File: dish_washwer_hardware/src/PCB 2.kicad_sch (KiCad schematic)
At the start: 25 parts, among them J18 Conn_02x07_Odd_Even, J19 SCREEN CONNECTOR, J20 Conn_01x10_Male, U12 TXS0108EPW, U13 EAST1616RGBA8, U14 EAST1616RGBA8, U15 MPR121QR2

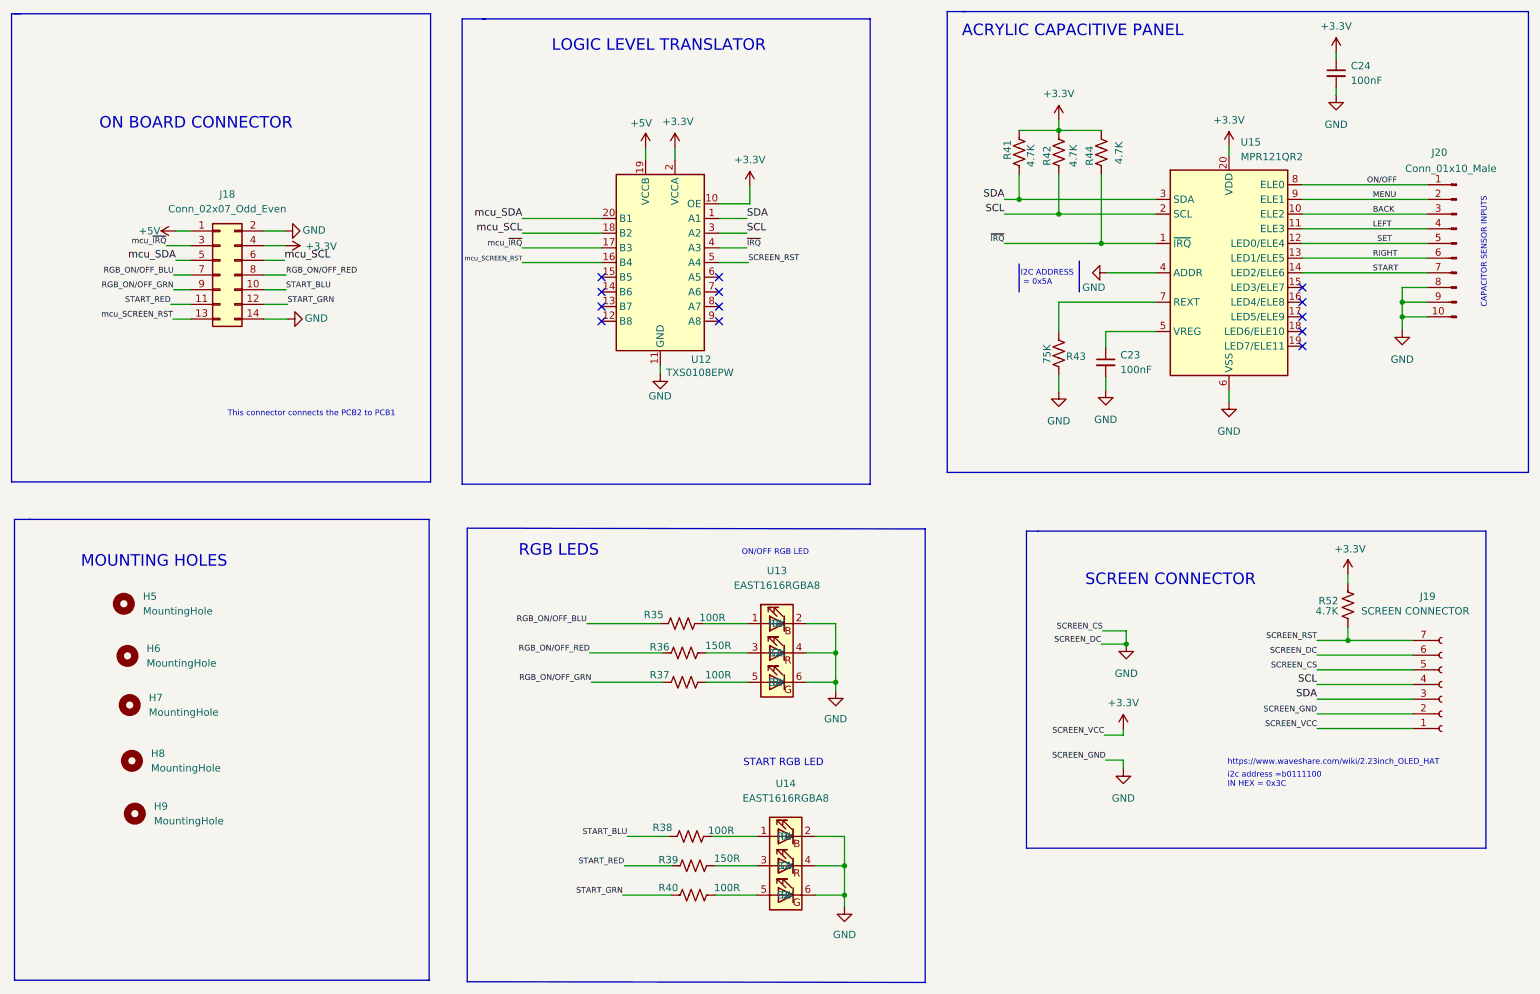
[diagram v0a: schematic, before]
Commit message: cheaper version layout
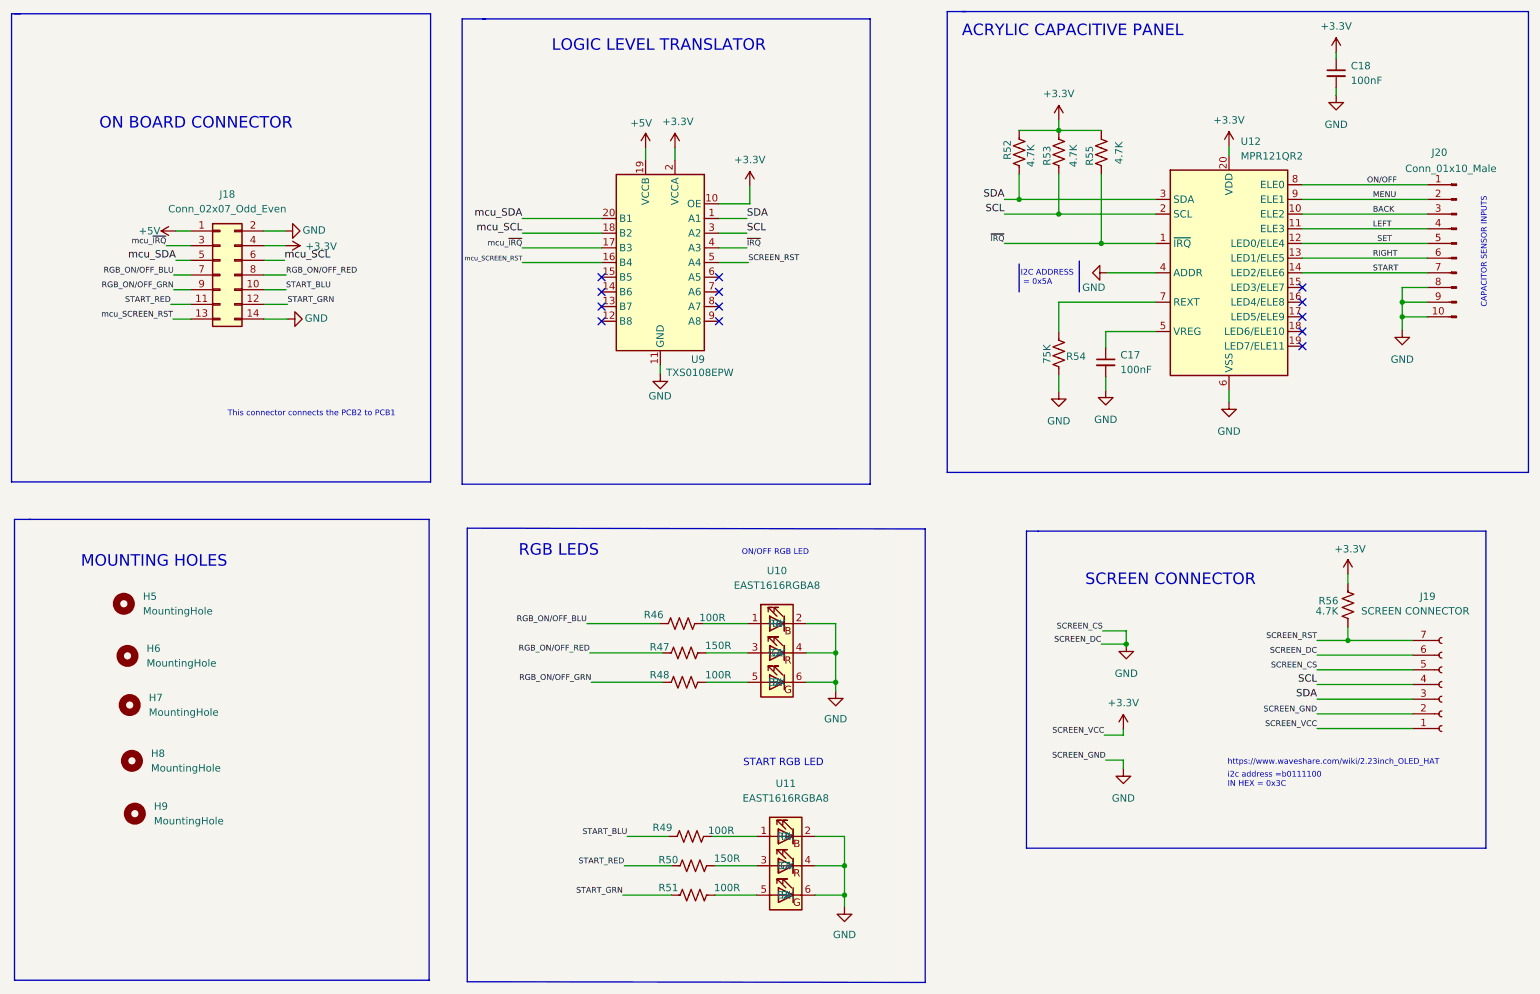
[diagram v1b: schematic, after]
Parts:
- renumbered C23 to C17, C24 to C18, R35 to R46, R36 to R47, R37 to R48, R38 to R49, R39 to R50, R40 to R51, R41 to R52, R42 to R53, R43 to R54, R44 to R55, R52 to R56, U13 to U10, U14 to U11, U15 to U12, U12 to U9
